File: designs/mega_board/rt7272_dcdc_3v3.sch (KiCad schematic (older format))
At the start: 14 parts

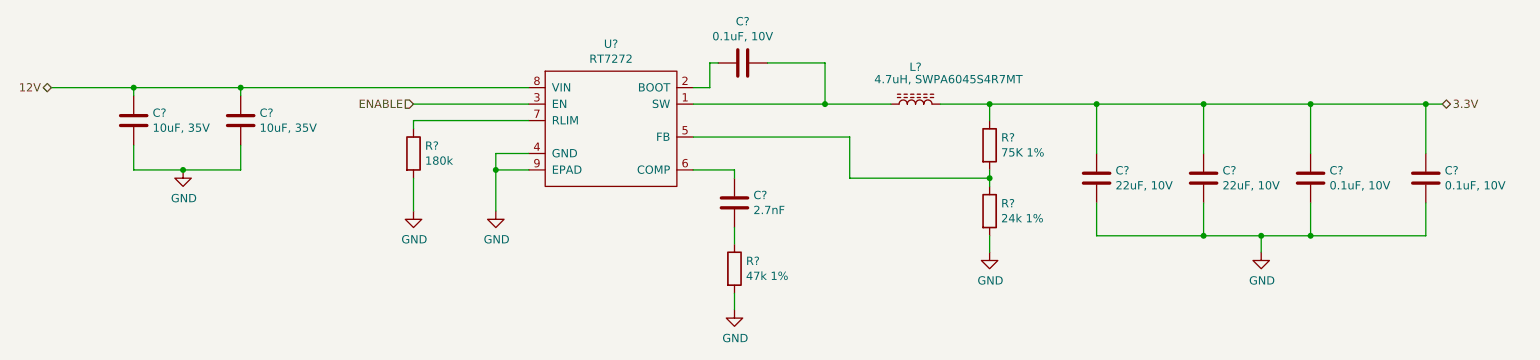
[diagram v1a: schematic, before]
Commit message: Enumerate components as is in eagle design.
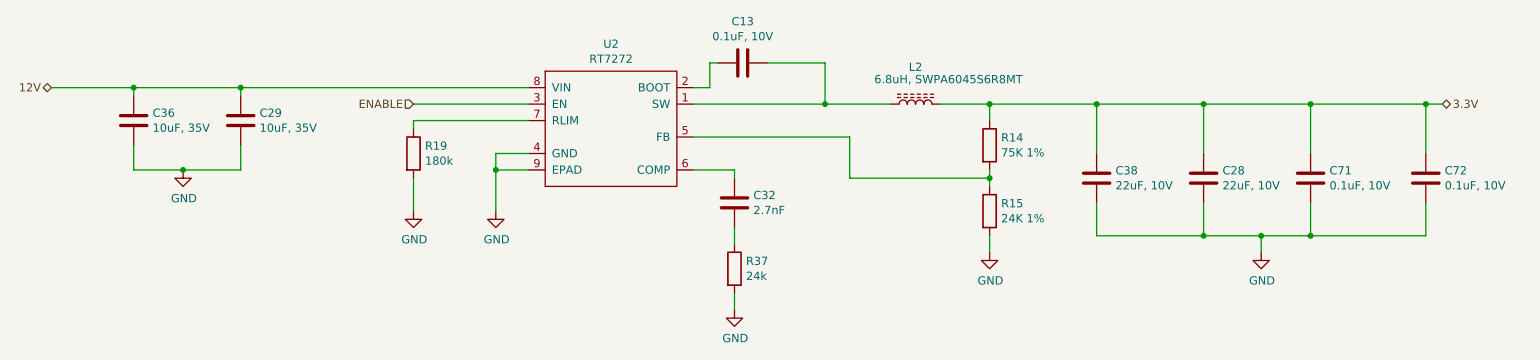
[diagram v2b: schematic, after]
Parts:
- C13, C32, C71, C72: renamed from C?; footprint (none) -> LibreRouter_MegaBoard:C0402
- C28, C29, C36, C38: renamed from C?; footprint (none) -> LibreRouter_MegaBoard:C0805
- L2: renamed from L?; value 4.7uH, SWPA6045S4R7MT -> 6.8uH, SWPA6045S6R8MT; footprint (none) -> LibreRouter_MegaBoard:SWPA6028S
- R14, R19: renamed from R?; footprint (none) -> LibreRouter_MegaBoard:R0402
- R15: renamed from R?; value 24k 1% -> 24K 1%; footprint (none) -> LibreRouter_MegaBoard:R0402
- R37: renamed from R?; value 47k 1% -> 24k; footprint (none) -> LibreRouter_MegaBoard:R0402
- U2: renamed from U?; footprint (none) -> LibreRouter_MegaBoard:RT8250-SOP8

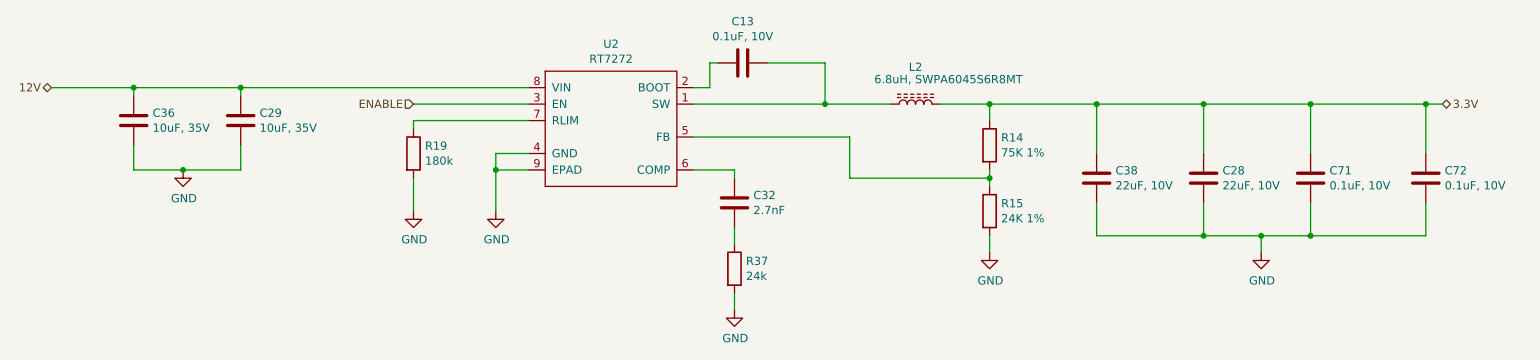
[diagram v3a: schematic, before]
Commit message: Add capacitor definito to BOM
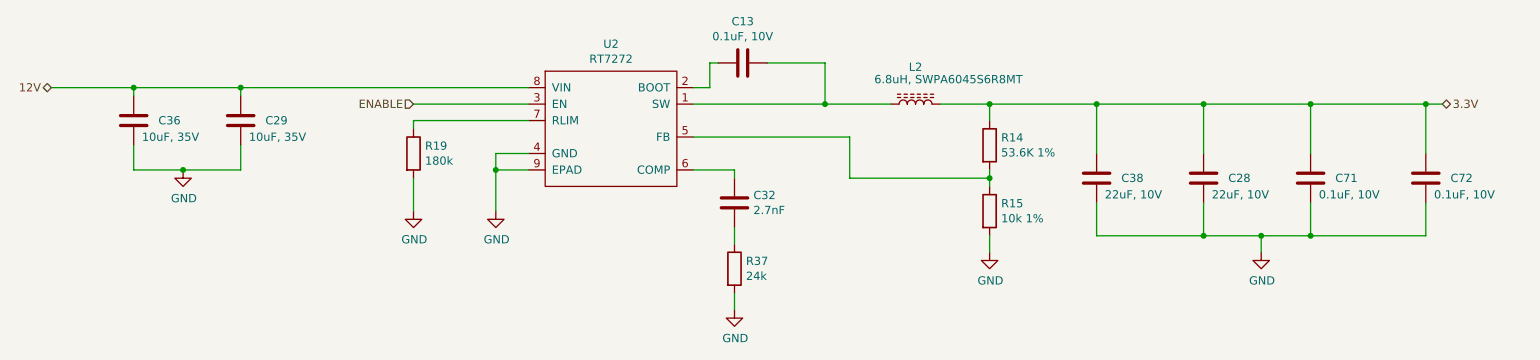
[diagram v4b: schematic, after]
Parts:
- C13, C71, C72: Manufacturer (none) -> Murata Electronics; Manufacturer PN (none) -> GCM155R71A104KA55D; Supplier (none) -> DigiKey; Supplier PN (none) -> 490-16434-6-ND
- C28, C38: Manufacturer (none) -> Murata Electronics; Manufacturer PN (none) -> GRM21BR61A226ME51L; Supplier (none) -> DigiKey; Supplier PN (none) -> 490-10511-6-ND
- C29, C36: Manufacturer (none) -> Murata Electronics; Manufacturer PN (none) -> GRM21BR6YA106ME43L; Supplier (none) -> DigiKey; Supplier PN (none) -> 490-10515-6-ND
- C32: Manufacturer (none) -> Murata Electronics; Manufacturer PN (none) -> GRM1557U1A272JA01D; Supplier (none) -> DigiKey; Supplier PN (none) -> 490-6275-6-ND
- R14: value 75K 1% -> 53.6K 1%
- R15: value 24K 1% -> 10k 1%
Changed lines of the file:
@@
 AR Path="/5D0328DE/5D42CD47/5D42D229" Ref="C29"  Part="1"
 AR Path="/5D0328DE/5D42E225/5D42D229" Ref="C15"  Part="1"
-F 0 "C29" H 3465 3496 50  0000 L CNN
-F 1 "10uF, 35V" H 3465 3405 50  0000 L CNN
+F 0 "C29" H 3500 3450 50  0000 L CNN
+F 1 "10uF, 35V" H 3400 3350 50  0000 L CNN
 F 2 "LibreRouter_MegaBoard:C0805" H 3388 3300 50  0001 C CNN
 F 3 "~" H 3350 3450 50  0001 C CNN
+F 4 "DigiKey" H 3350 3450 50  0001 C CNN "Supplier"
+F 5 "Murata Electronics" H 3350 3450 50  0001 C CNN "Manufacturer"
+F 6 "GRM21BR6YA106ME43L" H 3350 3450 50  0001 C CNN "Manufacturer PN"
+F 7 "490-10515-6-ND" H 3350 3450 50  0001 C CNN "Supplier PN"
 	1    3350 3450
 	1    0    0    -1
@@
 F 2 "LibreRouter_MegaBoard:C0402" H 6438 2950 50  0001 C CNN
 F 3 "~" H 6400 3100 50  0001 C CNN
+F 4 "Murata Electronics" H 6400 3100 50  0001 C CNN "Manufacturer"
+F 5 "GCM155R71A104KA55D" H 6400 3100 50  0001 C CNN "Manufacturer PN"
+F 6 "DigiKey" H 6400 3100 50  0001 C CNN "Supplier"
+F 7 "490-16434-6-ND" H 6400 3100 50  0001 C CNN "Supplier PN"
 	1    6400 3100
 	0    1    1    0
@@
 AR Path="/5D0328DE/5D42E225/5D42D571" Ref="R9"  Part="1"
 F 0 "R14" H 7970 3646 50  0000 L CNN
-F 1 "75K 1%" H 7970 3555 50  0000 L CNN
+F 1 "53.6K 1%" H 7970 3555 50  0000 L CNN
 F 2 "LibreRouter_MegaBoard:R0402" V 7830 3600 50  0001 C CNN
 F 3 "~" H 7900 3600 50  0001 C CNN
@@
 AR Path="/5D0328DE/5D42E225/5D42D5CB" Ref="R11"  Part="1"
 F 0 "R15" H 7970 4046 50  0000 L CNN
-F 1 "24K 1%" H 7970 3955 50  0000 L CNN
+F 1 "10k 1%" H 7970 3955 50  0000 L CNN
 F 2 "LibreRouter_MegaBoard:R0402" V 7830 4000 50  0001 C CNN
 F 3 "~" H 7900 4000 50  0001 C CNN
@@
 F 2 "LibreRouter_MegaBoard:C0402" H 6388 3800 50  0001 C CNN
 F 3 "~" H 6350 3950 50  0001 C CNN
+F 4 "DigiKey" H 6350 3950 50  0001 C CNN "Supplier"
+F 5 "GRM1557U1A272JA01D" H 6350 3950 50  0001 C CNN "Manufacturer PN"
+F 6 "490-6275-6-ND" H 6350 3950 50  0001 C CNN "Supplier PN"
+F 7 "Murata Electronics" H 6350 3950 50  0001 C CNN "Manufacturer"
 	1    6350 3950
 	-1   0    0    1
@@
 AR Path="/5D0328DE/5D42CD47/5D42DAC0" Ref="C38"  Part="1"
 AR Path="/5D0328DE/5D42E225/5D42DAC0" Ref="C17"  Part="1"
-F 0 "C38" H 8435 3754 50  0000 R CNN
-F 1 "22uF, 10V" H 8435 3845 50  0000 R CNN
+F 0 "C38" H 8400 3800 50  0000 R CNN
+F 1 "22uF, 10V" H 8500 3900 50  0000 R CNN
 F 2 "LibreRouter_MegaBoard:C0805" H 8588 3650 50  0001 C CNN
 F 3 "~" H 8550 3800 50  0001 C CNN
+F 4 "DigiKey" H 8550 3800 50  0001 C CNN "Supplier"
+F 5 "GRM21BR61A226ME51L" H 8550 3800 50  0001 C CNN "Manufacturer PN"
+F 6 "490-10511-6-ND" H 8550 3800 50  0001 C CNN "Supplier PN"
+F 7 "Murata Electronics" H 8550 3800 50  0001 C CNN "Manufacturer"
 	1    8550 3800
 	-1   0    0    1
@@
 AR Path="/5D0328DE/5D42CD47/5D42DBCD" Ref="C28"  Part="1"
 AR Path="/5D0328DE/5D42E225/5D42DBCD" Ref="C14"  Part="1"
-F 0 "C28" H 9085 3754 50  0000 R CNN
-F 1 "22uF, 10V" H 9085 3845 50  0000 R CNN
+F 0 "C28" H 9050 3800 50  0000 R CNN
+F 1 "22uF, 10V" H 9150 3900 50  0000 R CNN
 F 2 "LibreRouter_MegaBoard:C0805" H 9238 3650 50  0001 C CNN
 F 3 "~" H 9200 3800 50  0001 C CNN
+F 4 "DigiKey" H 9200 3800 50  0001 C CNN "Supplier"
+F 5 "GRM21BR61A226ME51L" H 9200 3800 50  0001 C CNN "Manufacturer PN"
+F 6 "490-10511-6-ND" H 9200 3800 50  0001 C CNN "Supplier PN"
+F 7 "Murata Electronics" H 9200 3800 50  0001 C CNN "Manufacturer"
 	1    9200 3800
 	-1   0    0    1
@@
 AR Path="/5D0328DE/5D42CD47/5D42DC2B" Ref="C71"  Part="1"
 AR Path="/5D0328DE/5D42E225/5D42DC2B" Ref="C91"  Part="1"
-F 0 "C71" H 9735 3754 50  0000 R CNN
-F 1 "0.1uF, 10V" H 9735 3845 50  0000 R CNN
+F 0 "C71" H 9700 3800 50  0000 R CNN
+F 1 "0.1uF, 10V" H 9800 3900 50  0000 R CNN
 F 2 "LibreRouter_MegaBoard:C0402" H 9888 3650 50  0001 C CNN
 F 3 "~" H 9850 3800 50  0001 C CNN
+F 4 "Murata Electronics" H 9850 3800 50  0001 C CNN "Manufacturer"
+F 5 "GCM155R71A104KA55D" H 9850 3800 50  0001 C CNN "Manufacturer PN"
+F 6 "DigiKey" H 9850 3800 50  0001 C CNN "Supplier"
+F 7 "490-16434-6-ND" H 9850 3800 50  0001 C CNN "Supplier PN"
 	1    9850 3800
 	-1   0    0    1
@@
 AR Path="/5D0328DE/5D42CD47/5D42DCB2" Ref="C72"  Part="1"
 AR Path="/5D0328DE/5D42E225/5D42DCB2" Ref="C92"  Part="1"
-F 0 "C72" H 10435 3754 50  0000 R CNN
-F 1 "0.1uF, 10V" H 10435 3845 50  0000 R CNN
+F 0 "C72" H 10400 3800 50  0000 R CNN
+F 1 "0.1uF, 10V" H 10500 3900 50  0000 R CNN
 F 2 "LibreRouter_MegaBoard:C0402" H 10588 3650 50  0001 C CNN
 F 3 "~" H 10550 3800 50  0001 C CNN
+F 4 "Murata Electronics" H 10550 3800 50  0001 C CNN "Manufacturer"
+F 5 "GCM155R71A104KA55D" H 10550 3800 50  0001 C CNN "Manufacturer PN"
+F 6 "DigiKey" H 10550 3800 50  0001 C CNN "Supplier"
+F 7 "490-16434-6-ND" H 10550 3800 50  0001 C CNN "Supplier PN"
 	1    10550 3800
 	-1   0    0    1
@@
 AR Path="/5D0328DE/5D42CD47/5D42DD90" Ref="#PWR0139"  Part="1"
 AR Path="/5D0328DE/5D42E225/5D42DD90" Ref="#PWR0145"  Part="1"
-F 0 "#PWR0145" H 7900 4000 50  0001 C CNN
+F 0 "#PWR0139" H 7900 4000 50  0001 C CNN
 F 1 "GND" H 7905 4077 50  0000 C CNN
 F 2 "" H 7900 4250 50  0001 C CNN
@@
 AR Path="/5D0328DE/5D42CD47/5D42DDBC" Ref="#PWR0140"  Part="1"
 AR Path="/5D0328DE/5D42E225/5D42DDBC" Ref="#PWR0146"  Part="1"
-F 0 "#PWR0146" H 9550 4000 50  0001 C CNN
+F 0 "#PWR0140" H 9550 4000 50  0001 C CNN
 F 1 "GND" H 9555 4077 50  0000 C CNN
 F 2 "" H 9550 4250 50  0001 C CNN
@@
 AR Path="/5D0328DE/5D42CD47/5D42FF27" Ref="#PWR0141"  Part="1"
 AR Path="/5D0328DE/5D42E225/5D42FF27" Ref="#PWR0147"  Part="1"
-F 0 "#PWR0147" H 6350 4350 50  0001 C CNN
+F 0 "#PWR0141" H 6350 4350 50  0001 C CNN
 F 1 "GND" H 6355 4427 50  0000 C CNN
 F 2 "" H 6350 4600 50  0001 C CNN
@@
 AR Path="/5D0328DE/5D42CD47/5D43058C" Ref="C36"  Part="1"
 AR Path="/5D0328DE/5D42E225/5D43058C" Ref="C19"  Part="1"
-F 0 "C36" H 2815 3496 50  0000 L CNN
-F 1 "10uF, 35V" H 2815 3405 50  0000 L CNN
+F 0 "C36" H 2850 3450 50  0000 L CNN
+F 1 "10uF, 35V" H 2750 3350 50  0000 L CNN
 F 2 "LibreRouter_MegaBoard:C0805" H 2738 3300 50  0001 C CNN
 F 3 "~" H 2700 3450 50  0001 C CNN
+F 4 "DigiKey" H 2700 3450 50  0001 C CNN "Supplier"
+F 5 "Murata Electronics" H 2700 3450 50  0001 C CNN "Manufacturer"
+F 6 "GRM21BR6YA106ME43L" H 2700 3450 50  0001 C CNN "Manufacturer PN"
+F 7 "490-10515-6-ND" H 2700 3450 50  0001 C CNN "Supplier PN"
 	1    2700 3450
 	1    0    0    -1
@@
 AR Path="/5D0328DE/5D42CD47/5D4322E2" Ref="#PWR0142"  Part="1"
 AR Path="/5D0328DE/5D42E225/5D4322E2" Ref="#PWR0148"  Part="1"
-F 0 "#PWR0148" H 3000 3500 50  0001 C CNN
+F 0 "#PWR0142" H 3000 3500 50  0001 C CNN
 F 1 "GND" H 3005 3577 50  0000 C CNN
 F 2 "" H 3000 3750 50  0001 C CNN
@@
 AR Path="/5D0328DE/5D42CD47/5D4323C5" Ref="#PWR0143"  Part="1"
 AR Path="/5D0328DE/5D42E225/5D4323C5" Ref="#PWR0149"  Part="1"
-F 0 "#PWR0149" H 4400 3750 50  0001 C CNN
+F 0 "#PWR0143" H 4400 3750 50  0001 C CNN
 F 1 "GND" H 4405 3827 50  0000 C CNN
 F 2 "" H 4400 4000 50  0001 C CNN
@@
 AR Path="/5D0328DE/5D42CD47/5D4323EC" Ref="#PWR0144"  Part="1"
 AR Path="/5D0328DE/5D42E225/5D4323EC" Ref="#PWR0150"  Part="1"
-F 0 "#PWR0150" H 4900 3750 50  0001 C CNN
+F 0 "#PWR0144" H 4900 3750 50  0001 C CNN
 F 1 "GND" H 4905 3827 50  0000 C CNN
 F 2 "" H 4900 4000 50  0001 C CNN

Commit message: Add DNP column. Add some connectors BOM definition.
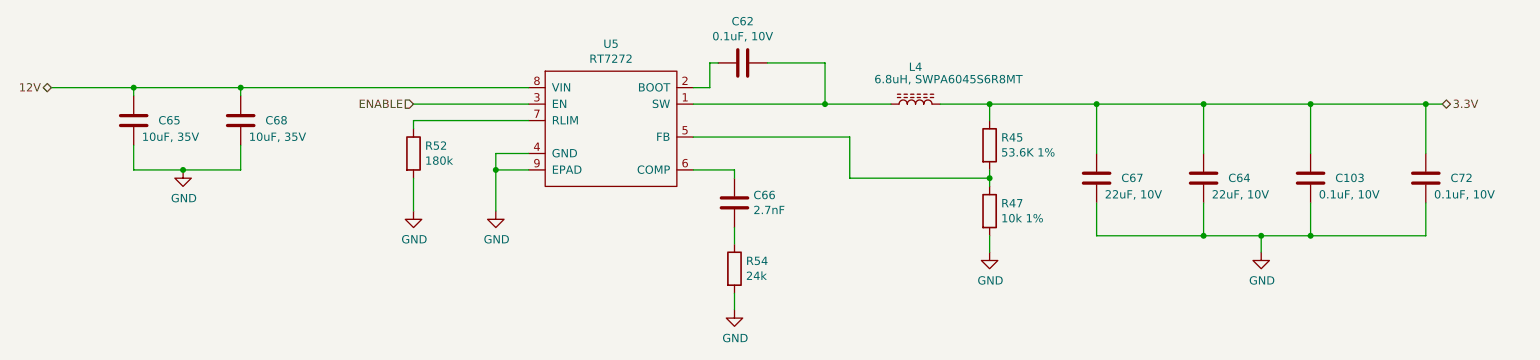
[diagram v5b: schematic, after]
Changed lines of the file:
@@
 AR Path="/5D0328DE/5D42E225/5D42D1B4" Ref="U6"  Part="1"
 AR Path="/5D42D1B4" Ref="U?"  Part="1"
-F 0 "U2" H 5600 4015 50  0000 C CNN
+F 0 "U5" H 5600 4015 50  0000 C CNN
 F 1 "RT7272" H 5600 3924 50  0000 C CNN
 F 2 "LibreRouter_MegaBoard:RT8250-SOP8" H 5600 3500 50  0001 C CNN
@@
 AR Path="/5D0328DE/5D42CD47/5D42D229" Ref="C29"  Part="1"
 AR Path="/5D0328DE/5D42E225/5D42D229" Ref="C15"  Part="1"
-F 0 "C29" H 3500 3450 50  0000 L CNN
+F 0 "C68" H 3500 3450 50  0000 L CNN
 F 1 "10uF, 35V" H 3400 3350 50  0000 L CNN
 F 2 "LibreRouter_MegaBoard:C0805" H 3388 3300 50  0001 C CNN
@@
 AR Path="/5D0328DE/5D42CD47/5D42D2DE" Ref="R19"  Part="1"
 AR Path="/5D0328DE/5D42E225/5D42D2DE" Ref="R58"  Part="1"
-F 0 "R19" H 4470 3696 50  0000 L CNN
+F 0 "R52" H 4470 3696 50  0000 L CNN
 F 1 "180k" H 4470 3605 50  0000 L CNN
 F 2 "LibreRouter_MegaBoard:R0402" V 4330 3650 50  0001 C CNN
@@
 AR Path="/5D0328DE/5D42CD47/5D42D3B9" Ref="L2"  Part="1"
 AR Path="/5D0328DE/5D42E225/5D42D3B9" Ref="L8"  Part="1"
-F 0 "L2" V 7675 3350 50  0000 C CNN
+F 0 "L4" V 7675 3350 50  0000 C CNN
 F 1 "6.8uH, SWPA6045S6R8MT" V 7600 3150 50  0000 C CNN
 F 2 "LibreRouter_MegaBoard:SWPA6028S" H 7450 3350 50  0001 C CNN
@@
 AR Path="/5D0328DE/5D42CD47/5D42D488" Ref="C13"  Part="1"
 AR Path="/5D0328DE/5D42E225/5D42D488" Ref="C12"  Part="1"
-F 0 "C13" V 6148 3100 50  0000 C CNN
+F 0 "C62" V 6148 3100 50  0000 C CNN
 F 1 "0.1uF, 10V" V 6239 3100 50  0000 C CNN
 F 2 "LibreRouter_MegaBoard:C0402" H 6438 2950 50  0001 C CNN
@@
 AR Path="/5D0328DE/5D42CD47/5D42D571" Ref="R14"  Part="1"
 AR Path="/5D0328DE/5D42E225/5D42D571" Ref="R9"  Part="1"
-F 0 "R14" H 7970 3646 50  0000 L CNN
+F 0 "R45" H 7970 3646 50  0000 L CNN
 F 1 "53.6K 1%" H 7970 3555 50  0000 L CNN
 F 2 "LibreRouter_MegaBoard:R0402" V 7830 3600 50  0001 C CNN
@@
 AR Path="/5D0328DE/5D42CD47/5D42D5CB" Ref="R15"  Part="1"
 AR Path="/5D0328DE/5D42E225/5D42D5CB" Ref="R11"  Part="1"
-F 0 "R15" H 7970 4046 50  0000 L CNN
+F 0 "R47" H 7970 4046 50  0000 L CNN
 F 1 "10k 1%" H 7970 3955 50  0000 L CNN
 F 2 "LibreRouter_MegaBoard:R0402" V 7830 4000 50  0001 C CNN
@@
 AR Path="/5D0328DE/5D42CD47/5D42D605" Ref="R37"  Part="1"
 AR Path="/5D0328DE/5D42E225/5D42D605" Ref="R59"  Part="1"
-F 0 "R37" H 6420 4396 50  0000 L CNN
+F 0 "R54" H 6420 4396 50  0000 L CNN
 F 1 "24k" H 6420 4305 50  0000 L CNN
 F 2 "LibreRouter_MegaBoard:R0402" V 6280 4350 50  0001 C CNN
@@
 AR Path="/5D0328DE/5D42CD47/5D42D659" Ref="C32"  Part="1"
 AR Path="/5D0328DE/5D42E225/5D42D659" Ref="C16"  Part="1"
-F 0 "C32" H 6235 3904 50  0000 R CNN
+F 0 "C66" H 6235 3904 50  0000 R CNN
 F 1 "2.7nF" H 6235 3995 50  0000 R CNN
 F 2 "LibreRouter_MegaBoard:C0402" H 6388 3800 50  0001 C CNN
@@
 AR Path="/5D0328DE/5D42CD47/5D42DAC0" Ref="C38"  Part="1"
 AR Path="/5D0328DE/5D42E225/5D42DAC0" Ref="C17"  Part="1"
-F 0 "C38" H 8400 3800 50  0000 R CNN
+F 0 "C67" H 8400 3800 50  0000 R CNN
 F 1 "22uF, 10V" H 8500 3900 50  0000 R CNN
 F 2 "LibreRouter_MegaBoard:C0805" H 8588 3650 50  0001 C CNN
@@
 AR Path="/5D0328DE/5D42CD47/5D42DBCD" Ref="C28"  Part="1"
 AR Path="/5D0328DE/5D42E225/5D42DBCD" Ref="C14"  Part="1"
-F 0 "C28" H 9050 3800 50  0000 R CNN
+F 0 "C64" H 9050 3800 50  0000 R CNN
 F 1 "22uF, 10V" H 9150 3900 50  0000 R CNN
 F 2 "LibreRouter_MegaBoard:C0805" H 9238 3650 50  0001 C CNN
@@
 AR Path="/5D0328DE/5D42CD47/5D42DC2B" Ref="C71"  Part="1"
 AR Path="/5D0328DE/5D42E225/5D42DC2B" Ref="C91"  Part="1"
-F 0 "C71" H 9700 3800 50  0000 R CNN
+F 0 "C103" H 9700 3800 50  0000 R CNN
 F 1 "0.1uF, 10V" H 9800 3900 50  0000 R CNN
 F 2 "LibreRouter_MegaBoard:C0402" H 9888 3650 50  0001 C CNN
@@
 AR Path="/5D0328DE/5D42CD47/5D43058C" Ref="C36"  Part="1"
 AR Path="/5D0328DE/5D42E225/5D43058C" Ref="C19"  Part="1"
-F 0 "C36" H 2850 3450 50  0000 L CNN
+F 0 "C65" H 2850 3450 50  0000 L CNN
 F 1 "10uF, 35V" H 2750 3350 50  0000 L CNN
 F 2 "LibreRouter_MegaBoard:C0805" H 2738 3300 50  0001 C CNN
